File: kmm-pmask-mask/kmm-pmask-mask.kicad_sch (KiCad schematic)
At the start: 0 parts

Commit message: preliminary schematic for mask
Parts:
- added C1, C10, C12, C14, C16, C18, C2, C20, C21, C22, C23, C3, C4, C5, C7: 100n, Capacitor_SMD:C_0201_0603Metric_Pad0.64x0.40mm_HandSolder, symbol Device:C
- added C11, C15, C19, C6: 4.7u, Capacitor_SMD:C_0402_1005Metric_Pad0.74x0.62mm_HandSolder, symbol Device:C
- added C13, C17, C8, C9: 10u, Capacitor_SMD:C_0402_1005Metric_Pad0.74x0.62mm_HandSolder, symbol Device:C
- added J1: F31L-1A7H1-11030, symbol Connector:Conn_01x30_Socket
- added U1, U5, U6, U7: MS5611-01BA, Package_LGA:LGA-8_3x5mm_P1.25mm, symbol Sensor_Pressure:MS5611-01BA
- added U10, U2, U8, U9: MAX30101EFD_T, kmm-pmask:MAX30101EFD_T, symbol kmm-pmask:MAX30101EFD_T
- added U11, U12, U3: SHT40-AD1B-R3, Sensor_Humidity:Sensirion_DFN-4_1.5x1.5mm_P0.8mm_SHT4x_NoCentralPad, symbol Sensor_Humidity:SHT4x
- added U13, U14, U4: TMP117MAIDRVR, Package_SON:WSON-6-1EP_2x2mm_P0.65mm_EP1x1.6mm, symbol Sensor_Temperature:TMP117xxDRV
- added U15: TCA9546APW, Package_SO:TSSOP-16_4.4x5mm_P0.65mm, symbol Interface_Expansion:TCA9546APW
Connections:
- new net: U4.4 (ADD0), U4.6 (SDA)
- new net +1V8: C11.1, C12.1, C15.1, C16.1, C19.1, C20.1, C5.1, C6.1, U10.10 (VLED+), U10.9 (VLED+), U2.10 (VLED+), U2.9 (VLED+), U8.10 (VLED+), U8.9 (VLED+), U9.10 (VLED+), U9.9 (VLED+)
- new net +3.3V: C1.1, C2.1, C21.1, C22.1, C23.1, C3.1, C4.1, U1.1 (VDD), U1.2 (PS), U11.3 (VDD), U12.3 (VDD), U13.4 (ADD0), U13.5 (V+), U14.5 (V+), U15.16 (VCC), U3.3 (VDD), U4.5 (V+), U5.1 (VDD), U5.2 (PS), U6.1 (VDD), U6.2 (PS), U7.1 (VDD), U7.2 (PS)
- new net +5V: C10.1, C13.1, C14.1, C17.1, C18.1, C7.1, C8.1, C9.1, U10.11 (VDD), U2.11 (VDD), U8.11 (VDD), U9.11 (VDD)
- new net GND: C1.2, C10.2, C11.2, C12.2, C13.2, C14.2, C15.2, C16.2, C17.2, C18.2, C19.2, C2.2, C20.2, C21.2, C22.2, C23.2, C3.2, C4.2, C5.2, C6.2, C7.2, C8.2, C9.2, U1.3 (GND), U1.4 (CSB), U1.5 (CSB), U10.12 (GND), U10.4 (PGND), U11.4 (VSS), U12.4 (VSS), U13.2 (GND), U14.2 (GND), U14.4 (ADD0), U15.1 (A0), U15.13 (A2), U15.2 (A1), U15.8 (GND), U2.12 (GND), U2.4 (PGND), U3.4 (VSS), U4.2 (GND), U5.3 (GND), U5.4 (CSB), U5.5 (CSB), U6.3 (GND), U6.4 (CSB), U6.5 (CSB), U7.3 (GND), U7.4 (CSB), U7.5 (CSB), U8.12 (GND), U8.4 (PGND), U9.12 (GND), U9.4 (PGND)
- no-connect marks 0 -> 7
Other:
- note added: "A0-2 shorted to GND I2C addr 0x70"
- note added: "ADDR0 shorted to GND I2C addr 0x4A"
- note added: "ADDR0 shorted to SDA I2C addr 0x4C"
- note added: "ADDR0 shorted to VCC I2C addr 0x4B"
- note added: "CSB pulled low I2C addr 0x77"
- note added: "I2C addr 0x44"
- note added: "I2C bus 3.3 V PU tolerant I2C W/R addr: 0xAE/0xAF"
- note added: "PS pulled high: I2C Enabled"
- note added: "Place caps close to IC"
- company: (none) -> Ka Moamoa Lab, Georgia Institute of Technology
- title: (none) -> Flexible Patient Monitoring Mask Insert

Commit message: preliminary placement for mask sensors
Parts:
- J1: footprint (none) -> kmm-pmask:AMPHENOL_F31L-1A7H1-11030
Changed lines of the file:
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@@
 			)
 		)
-		(property "Footprint" ""
+		(property "Footprint" "kmm-pmask:AMPHENOL_F31L-1A7H1-11030"
 			(at 383.54 173.99 0)
 			(hide yes)

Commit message: fix incorrect I2C address note
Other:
- note added: "I2C bus 3.3 V PU tolerant I2C addr: 0x57"
- note removed: "I2C bus 3.3 V PU tolerant I2C W/R addr: 0xAE/0xAF"
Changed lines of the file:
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@@
 		)
 	)
-	(text "I2C bus 3.3 V PU tolerant\n\nI2C W/R addr:\n0xAE/0xAF"
+	(text "I2C bus 3.3 V PU tolerant\n\nI2C addr: 0x57"
 		(exclude_from_sim no)
 		(at 162.56 44.45 0)
@@
 		)
 	)
-	(text "I2C bus 3.3 V PU tolerant\n\nI2C W/R addr:\n0xAE/0xAF"
+	(text "I2C bus 3.3 V PU tolerant\n\nI2C addr: 0x57"
 		(exclude_from_sim no)
 		(at 165.1 128.27 0)
@@
 		)
 	)
-	(text "I2C bus 3.3 V PU tolerant\n\nI2C W/R addr:\n0xAE/0xAF"
+	(text "I2C bus 3.3 V PU tolerant\n\nI2C addr: 0x57"
 		(exclude_from_sim no)
 		(at 166.37 172.72 0)
@@
 		)
 	)
-	(text "I2C bus 3.3 V PU tolerant\n\nI2C W/R addr:\n0xAE/0xAF"
+	(text "I2C bus 3.3 V PU tolerant\n\nI2C addr: 0x57"
 		(exclude_from_sim no)
 		(at 163.83 86.36 0)

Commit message: Mostly annotate schematic
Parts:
- added C24, C25, C26: 100n, Capacitor_SMD:C_0201_0603Metric_Pad0.64x0.40mm_HandSolder, symbol Device:C
- added R1, R2, R3, R4, R5, R6, R7, R8: 4.7k, Resistor_SMD:R_0201_0603Metric_Pad0.64x0.40mm_HandSolder, symbol Device:R
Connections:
- net +3.3V: now also C24.1, C25.1, C26.1, R1.1, R2.1, R3.1, R4.1, R5.1, R6.1, R7.1, R8.1; no longer U13.4 (ADD0)
- net GND: now also U13.4 (ADD0), U4.4 (ADD0), C24.2, C25.2, C26.2
- net I2C2_SCL: now reaches U8.2 (SCL)
- net I2C2_SCL: now also U13.1 (SCL), U15.10 (SC2), U6.8 (SCLK), R6.2
- net I2C2_SDA: now reaches U8.3 (SDA)
- net I2C2_SDA: now also U13.6 (SDA), U15.9 (SD2), U6.7 (SDI/SDA), R5.2
- net I2C3_SCL: now reaches U10.2 (SCL)
- net I2C3_SCL: now also U14.1 (SCL), U15.12 (SC3), U7.8 (SCLK), R8.2
- net I2C3_SDA: now reaches U10.3 (SDA)
- net I2C3_SDA: now also U14.6 (SDA), U15.11 (SD3), U7.7 (SDI/SDA), R7.2
- net I2C0_SCL: now reaches U2.2 (SCL)
- net I2C0_SCL: now also U1.8 (SCLK), U15.5 (SC0), R2.2
- net I2C0_SDA: now reaches U2.3 (SDA)
- net I2C0_SDA: now also U1.7 (SDI/SDA), U15.4 (SD0), R1.2
- net I2C1_SCL: now reaches U4.1 (SCL)
- net I2C1_SCL: now also U11.2 (SCL), U12.2 (SCL), U15.7 (SC1), U3.2 (SCL), U5.8 (SCLK), U9.2 (SCL), R4.2
- net I2C1_SDA: now reaches U4.6 (SDA)
- net I2C1_SDA: now also U11.1 (SDA), U12.1 (SDA), U15.6 (SD1), U3.1 (SDA), U5.7 (SDI/SDA), U9.3 (SDA), R3.2; no longer U4.4 (ADD0)
- net I2C_M_SCL: now reaches U15.14 (SCL)
- net I2C_M_SDA: now reaches U15.15 (SDA)
- net ~{I2C_M_RST}: now reaches U15.3 (~{RESET})
- net +1V8 renamed +1.8V
- no-connect marks 7 -> 11
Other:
- note added: "(Final placement may differ)"
- note added: "1:4 I2C Bus Switch"
- note added: "Barometric Pressure Sensor"
- note added: "Combination Humidity/Temperature Sensor"
- note added: "Combination Pulse Oximeter/Heart-Rate Sensor"
- note added: "External FFC Connection"
- note added: "External pull-ups required on MCU Side"
- note added: "I2C Address Table"
- note added: "I2C Bus Group A"
- note added: "I2C Bus Group B"
- note added: "I2C Bus Group C"
- note added: "I2C Bus Group D"
- note added: "I2C bus 3.3 V tolerant I2C addr 0x57"
- note added: "Maximum Current Consumption per Power Rail, Other"
- note added: "Maximum Current Consumption per Power Rail, Sensors"
- note added: "Notes on I2C Bus Groupings"
- note added: "Notes on Power Supply"
- note added: "PS pulled high I2C Enabled"
- note added: "Recommended Supply Current per Power Rail, Entire Board"
- note added: "Temperature Sensor"
- note added: "This section will be completed when component placement has been confirmed by the customer."
- note removed: "ADDR0 shorted to SDA I2C addr 0x4C"
- note removed: "ADDR0 shorted to VCC I2C addr 0x4B"
- note removed: "I2C bus 3.3 V PU tolerant I2C addr: 0x57"
- moved on the sheet: C1, C10, C11, C12, C13, C14, C15, C16, C17, C18, C19, C2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

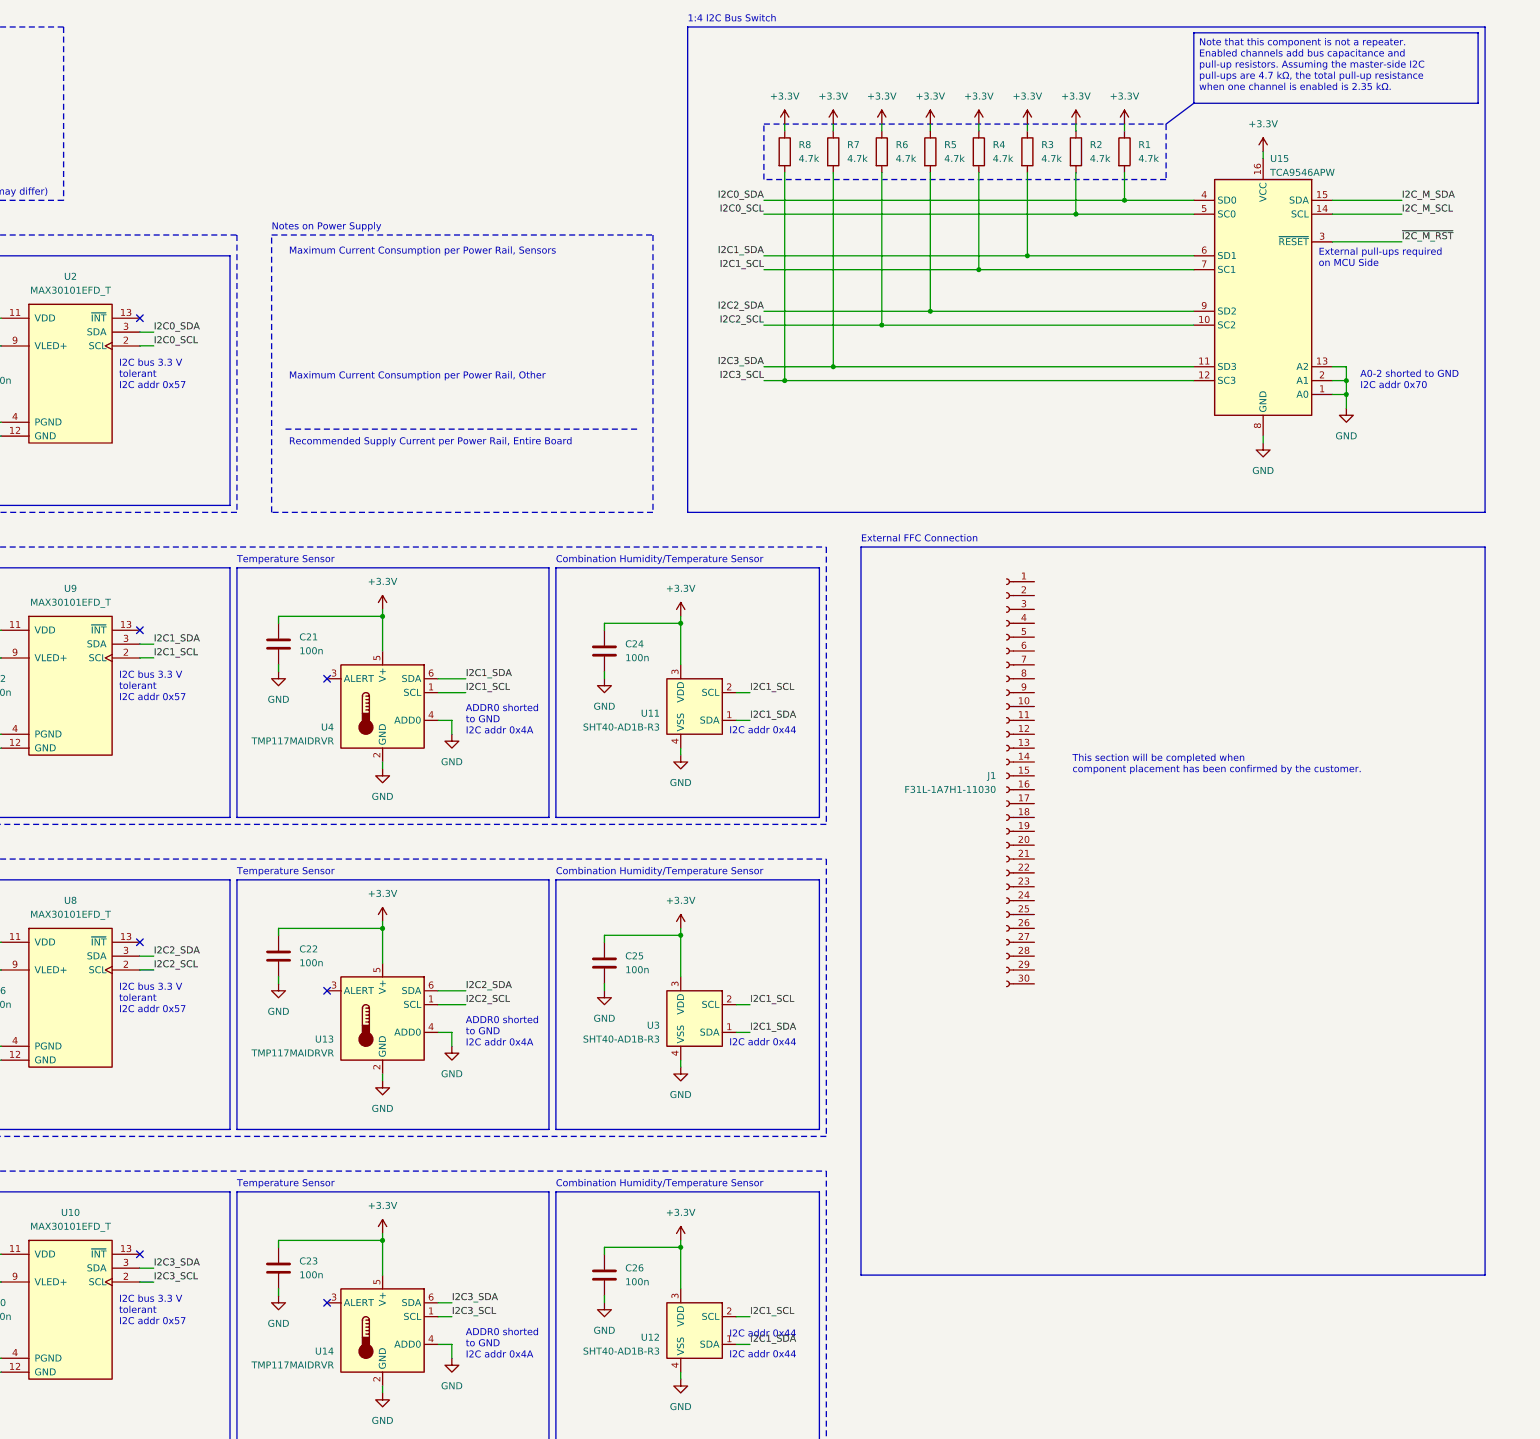
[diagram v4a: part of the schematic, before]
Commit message: Add test points
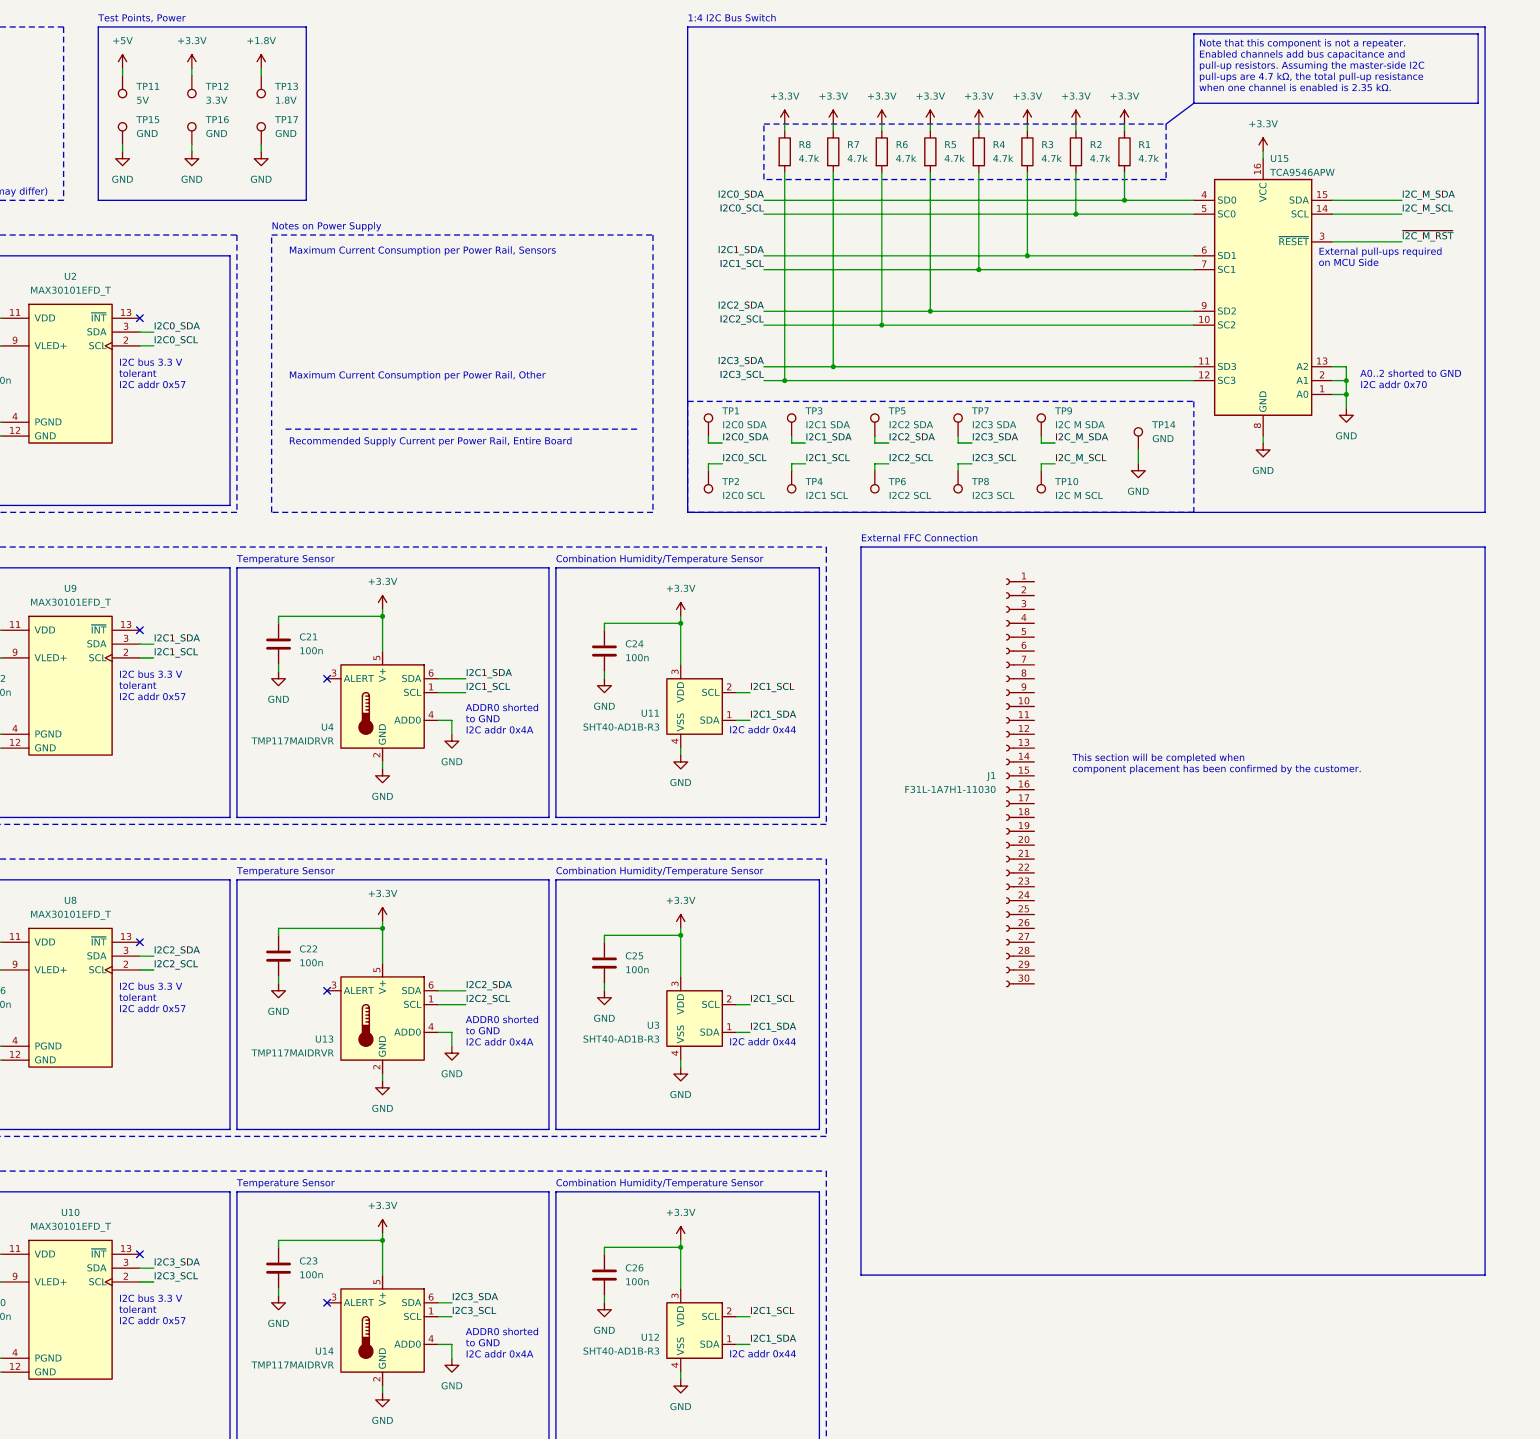
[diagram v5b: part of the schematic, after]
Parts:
- added TP1: I2C0 SDA, TestPoint:TestPoint_Pad_1.5x1.5mm, symbol Connector:TestPoint
- added TP10: I2C M SCL, TestPoint:TestPoint_Pad_1.5x1.5mm, symbol Connector:TestPoint
- added TP11: 5V, TestPoint:TestPoint_Pad_1.5x1.5mm, symbol Connector:TestPoint
- added TP12: 3.3V, TestPoint:TestPoint_Pad_1.5x1.5mm, symbol Connector:TestPoint
- added TP13: 1.8V, TestPoint:TestPoint_Pad_1.5x1.5mm, symbol Connector:TestPoint
- added TP14, TP15, TP16, TP17: GND, TestPoint:TestPoint_Pad_1.5x1.5mm, symbol Connector:TestPoint
- added TP2: I2C0 SCL, TestPoint:TestPoint_Pad_1.5x1.5mm, symbol Connector:TestPoint
- added TP3: I2C1 SDA, TestPoint:TestPoint_Pad_1.5x1.5mm, symbol Connector:TestPoint
- added TP4: I2C1 SCL, TestPoint:TestPoint_Pad_1.5x1.5mm, symbol Connector:TestPoint
- added TP5: I2C2 SDA, TestPoint:TestPoint_Pad_1.5x1.5mm, symbol Connector:TestPoint
- added TP6: I2C2 SCL, TestPoint:TestPoint_Pad_1.5x1.5mm, symbol Connector:TestPoint
- added TP7: I2C3 SDA, TestPoint:TestPoint_Pad_1.5x1.5mm, symbol Connector:TestPoint
- added TP8: I2C3 SCL, TestPoint:TestPoint_Pad_1.5x1.5mm, symbol Connector:TestPoint
- added TP9: I2C M SDA, TestPoint:TestPoint_Pad_1.5x1.5mm, symbol Connector:TestPoint
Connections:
- net +1.8V: now also TP13.1
- net +3.3V: now also TP12.1
- net +5V: now also TP11.1
- net GND: now also TP14.1, TP15.1, TP16.1, TP17.1
- net I2C0_SCL: now also TP2.1
- net I2C0_SDA: now also TP1.1
- net I2C1_SCL: now also TP4.1
- net I2C1_SDA: now also TP3.1
- net I2C2_SCL: now also TP6.1
- net I2C2_SDA: now also TP5.1
- net I2C3_SCL: now also TP8.1
- net I2C3_SDA: now also TP7.1
- net I2C_M_SCL: now also TP10.1
- net I2C_M_SDA: now also TP9.1
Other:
- note added: "A0..2 shorted to GND I2C addr 0x70"
- note added: "Test Points, Power"
- note removed: "A0-2 shorted to GND I2C addr 0x70"

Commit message: add extra decoupling caps, pull-ups to placement
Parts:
- added C27: 100n, Capacitor_SMD:C_0201_0603Metric_Pad0.64x0.40mm_HandSolder, symbol Device:C
- TP1, TP10, TP11, TP12, TP13, TP14, TP15, TP16, TP17, TP2, TP3, TP4, TP5, TP6, TP7, TP8, TP9: footprint TestPoint:TestPoint_Pad_1.5x1.5mm -> TestPoint:TestPoint_Pad_D1.5mm
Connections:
- net +3.3V: now also C27.1
- net GND: now also C27.2
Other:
- note added: "External pull-ups required on MCU Side SCL up to 400 kHz (I2C Fast Mode)"
- note removed: "External pull-ups required on MCU Side"

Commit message: initial routing
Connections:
- net +1.8V: now also C10.1, C14.1, C18.1, C7.1, J1.24 (Pin_24), J1.7 (Pin_7), U10.11 (VDD), U2.11 (VDD), U8.11 (VDD), U9.11 (VDD); no longer C12.1, C16.1, C20.1, C5.1, U10.10 (VLED+), U10.9 (VLED+), U2.10 (VLED+), U2.9 (VLED+), U8.10 (VLED+), U8.9 (VLED+), U9.10 (VLED+), U9.9 (VLED+)
- net +3.3V: now also J1.26 (Pin_26), J1.27 (Pin_27), J1.4 (Pin_4), J1.5 (Pin_5)
- net +5V: now also C12.1, C16.1, C20.1, C5.1, J1.1 (Pin_1), J1.2 (Pin_2), J1.29 (Pin_29), J1.30 (Pin_30), U10.10 (VLED+), U10.9 (VLED+), U2.10 (VLED+), U2.9 (VLED+), U8.10 (VLED+), U8.9 (VLED+), U9.10 (VLED+), U9.9 (VLED+); no longer C10.1, C14.1, C18.1, C7.1, U10.11 (VDD), U2.11 (VDD), U8.11 (VDD), U9.11 (VDD)
- net GND: now also J1.12 (Pin_12), J1.15 (Pin_15), J1.16 (Pin_16), J1.19 (Pin_19), J1.23 (Pin_23), J1.25 (Pin_25), J1.28 (Pin_28), J1.3 (Pin_3), J1.6 (Pin_6), J1.8 (Pin_8)
- net I2C0_SCL: now also U11.2 (SCL), U4.1 (SCL), U5.8 (SCLK), U9.2 (SCL); no longer U1.8 (SCLK), U2.2 (SCL)
- net I2C0_SDA: now also U11.1 (SDA), U4.6 (SDA), U5.7 (SDI/SDA), U9.3 (SDA); no longer U1.7 (SDI/SDA), U2.3 (SDA)
- net I2C1_SCL: now also U1.8 (SCLK), U2.2 (SCL); no longer U11.2 (SCL), U12.2 (SCL), U3.2 (SCL), U4.1 (SCL), U5.8 (SCLK), U9.2 (SCL)
- net I2C1_SDA: now also U1.7 (SDI/SDA), U2.3 (SDA); no longer U11.1 (SDA), U12.1 (SDA), U3.1 (SDA), U4.6 (SDA), U5.7 (SDI/SDA), U9.3 (SDA)
- net I2C2_SCL: now also U10.2 (SCL), U12.2 (SCL), U14.1 (SCL), U7.8 (SCLK); no longer U13.1 (SCL), U6.8 (SCLK), U8.2 (SCL)
- net I2C2_SDA: now also U10.3 (SDA), U12.1 (SDA), U14.6 (SDA), U7.7 (SDI/SDA); no longer U13.6 (SDA), U6.7 (SDI/SDA), U8.3 (SDA)
- net I2C3_SCL: now also U13.1 (SCL), U3.2 (SCL), U6.8 (SCLK), U8.2 (SCL); no longer U10.2 (SCL), U14.1 (SCL), U7.8 (SCLK)
- net I2C3_SDA: now also U13.6 (SDA), U3.1 (SDA), U6.7 (SDI/SDA), U8.3 (SDA); no longer U10.3 (SDA), U14.6 (SDA), U7.7 (SDI/SDA)
- net I2C_M_SCL: now also J1.14 (Pin_14), J1.17 (Pin_17)
- net I2C_M_SDA: now also J1.13 (Pin_13), J1.18 (Pin_18)
- net ~{I2C_M_RST}: now also J1.11 (Pin_11), J1.20 (Pin_20)
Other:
- note removed: "This section will be completed when component placement has been confirmed by the customer."
- moved on the sheet: J1

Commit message: Schematic annotations, power flags
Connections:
- net PRESEN0: now reaches J1.10 (Pin_10)
- net PRESEN0: now also J1.9 (Pin_9)
- net PRESEN1: now reaches J1.21 (Pin_21)
- net PRESEN1: now also J1.22 (Pin_22)
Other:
- note added: "(Placement may differ)"
- note added: "I2C (pull-ups required) 400 kHz (FM) max"
- note added: "Line of symmetry"
- note added: "Power Flags"
- note added: "Power Input 5.0V: 1.0A max 3.3V: 1.0A max 1.8V: 0.5A max"
- note added: "Presence Detection"
- note added: "Switch Mapping"
- note removed: "(Final placement may differ)"
- moved on the sheet: J1, TP11, TP12, TP13, TP15, TP16, TP17
